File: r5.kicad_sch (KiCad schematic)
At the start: 73 parts, among them J1 Conn_01x04, U1 LMZ22005, U10 74368PW, U100 Pico, U2 74LS365, U20 DRV8871DDA, U3 GY-BNO08X, U30 DRV8871DDA, U4 PI22, U40 DRV8871DDA, U5 SDD1309, U50 DRV8871DDA, U6 3X3HEADER, U60 DRV8871DDA, U70 DRV8871DDA, U80 PCA9685PW, X1 Conn_01x02, X2 Conn_01x02, X20 Conn_01x06, X30 Conn_01x06, X40 Conn_01x06, X50 Conn_01x06, X60 Conn_01x06, X70 Conn_01x06, X81 4X3HEADER

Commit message: wip
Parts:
- added R15, R16, R17: 100k, Resistor_SMD:R_0805_2012Metric_Pad1.20x1.40mm_HandSolder, symbol Device:R
- added SW1, SW2, SW3, SW4: SW_SPDT, _r5:SW_Slide_1P2T_CK_OS102011MS2Q, symbol Switch:SW_SPDT
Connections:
- net +3.3V: now also R15.1, R16.1, R17.1
- net +BATT: now also SW1.3 (C); no longer R11.1
- net GND: now also SW3.1 (A), SW4.3 (C)
- net INBUTTON: now also R17.2
- net MENABLE: now also SW2.2 (B); no longer R10.2, U10.1 (OEa), U10.15 (OEb), U2.1 (E1), U2.15 (E2)
- net at U80.23 (~{OE}): now also R15.2, SW4.2 (B)
- net INWIFI: now reaches U4.11 (GPIO17)
- net INWIFI: now also R16.2, SW3.2 (B)
- new net: R10.2, SW2.3 (C), U10.1 (OEa), U10.15 (OEb), U2.1 (E1), U2.15 (E2)
- new net: R11.1, SW1.2 (B)
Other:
- moved on the sheet: C1, C2, R10, R11, R12, R13

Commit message: wip
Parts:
- D91: footprint LED_SMD:LED_WS2812B_PLCC4_5.0x5.0mm_P3.2mm -> LED_SMD:LED_WS2812B-2020_PLCC4_2.0x2.0mm; JLCPCB Rotation Offset (none) -> 0; LCSC Part # (none) -> C965555
- R10, R14, R15, R16, R17, R3: JLCPCB Rotation Offset (none) -> 0; LCSC Part # (none) -> C913998
- U20, U30, U40, U50, U60, U70: JLCPCB Rotation Offset (none) -> 0; LCSC Part # (none) -> C75864
- U80: JLCPCB Rotation Offset (none) -> 0; LCSC Part # (none) -> C2678753
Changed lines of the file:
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@@
       (effects (font (size 1.27 1.27)) hide)
     )
+    (property "JLCPCB Rotation Offset" "0" (at 355.6 364.49 0)
+      (effects (font (size 1.27 1.27)) hide)
+    )
+    (property "LCSC Part #" "C75864" (at 355.6 364.49 0)
+      (effects (font (size 1.27 1.27)) hide)
+    )
     (pin "6")
     (pin "2")
@@
       (effects (font (size 1.27 1.27)) hide)
     )
+    (property "JLCPCB Rotation Offset" "0" (at 355.6 400.05 0)
+      (effects (font (size 1.27 1.27)) hide)
+    )
+    (property "LCSC Part #" "C75864" (at 355.6 400.05 0)
+      (effects (font (size 1.27 1.27)) hide)
+    )
     (pin "1")
     (pin "7")
@@
       (effects (font (size 1.27 1.27)) hide)
     )
+    (property "JLCPCB Rotation Offset" "0" (at 411.48 327.66 0)
+      (effects (font (size 1.27 1.27)) hide)
+    )
+    (property "LCSC Part #" "C75864" (at 411.48 327.66 0)
+      (effects (font (size 1.27 1.27)) hide)
+    )
     (pin "1")
     (pin "2")
@@
       (effects (font (size 1.27 1.27)) hide)
     )
+    (property "JLCPCB Rotation Offset" "0" (at 411.48 363.22 0)
+      (effects (font (size 1.27 1.27)) hide)
+    )
+    (property "LCSC Part #" "C75864" (at 411.48 363.22 0)
+      (effects (font (size 1.27 1.27)) hide)
+    )
     (pin "7")
     (pin "5")
@@
       (effects (font (size 1.27 1.27)) hide)
     )
+    (property "JLCPCB Rotation Offset" "0" (at 411.48 400.05 0)
+      (effects (font (size 1.27 1.27)) hide)
+    )
+    (property "LCSC Part #" "C75864" (at 411.48 400.05 0)
+      (effects (font (size 1.27 1.27)) hide)
+    )
     (pin "7")
     (pin "6")
@@
       (effects (font (size 1.27 1.27)) hide)
     )
+    (property "LCSC Part #" "C2678753" (at 577.85 381 0)
+      (effects (font (size 1.27 1.27)) hide)
+    )
+    (property "JLCPCB Rotation Offset" "0" (at 577.85 381 0)
+      (effects (font (size 1.27 1.27)) hide)
+    )
     (pin "9")
     (pin "20")
@@
       (effects (font (size 1.27 1.27)) hide)
     )
+    (property "JLCPCB Rotation Offset" "0" (at 257.81 267.97 0)
+      (effects (font (size 1.27 1.27)) hide)
+    )
+    (property "LCSC Part #" "C913998" (at 257.81 267.97 0)
+      (effects (font (size 1.27 1.27)) hide)
+    )
     (pin "2")
     (pin "1")
@@
       (effects (font (size 1.27 1.27)) hide)
     )
+    (property "JLCPCB Rotation Offset" "0" (at 355.6 328.93 0)
+      (effects (font (size 1.27 1.27)) hide)
+    )
+    (property "LCSC Part #" "C75864" (at 355.6 328.93 0)
+      (effects (font (size 1.27 1.27)) hide)
+    )
     (pin "9")
     (pin "5")
@@
       (effects (font (size 1.27 1.27)) hide)
     )
+    (property "JLCPCB Rotation Offset" "0" (at 468.63 274.32 0)
+      (effects (font (size 1.27 1.27)) hide)
+    )
+    (property "LCSC Part #" "C913998" (at 468.63 274.32 0)
+      (effects (font (size 1.27 1.27)) hide)
+    )
     (pin "1")
     (pin "2")
@@
       (effects (font (size 1.27 1.27)) hide)
     )
-    (property "Footprint" "LED_SMD:LED_WS2812B_PLCC4_5.0x5.0mm_P3.2mm" (at 251.46 420.37 0)
+    (property "Footprint" "LED_SMD:LED_WS2812B-2020_PLCC4_2.0x2.0mm" (at 251.46 420.37 0)
       (effects (font (size 1.27 1.27)) hide)
     )
@@
       (effects (font (size 1.27 1.27)) hide)
     )
+    (property "JLCPCB Rotation Offset" "0" (at 251.46 420.37 0)
+      (effects (font (size 1.27 1.27)) hide)
+    )
+    (property "LCSC Part #" "C965555" (at 251.46 420.37 0)
+      (effects (font (size 1.27 1.27)) hide)
+    )
     (pin "1")
     (pin "4")
@@
       (effects (font (size 1.27 1.27)) hide)
     )
+    (property "JLCPCB Rotation Offset" "0" (at 546.1 345.44 0)
+      (effects (font (size 1.27 1.27)) hide)
+    )
+    (property "LCSC Part #" "C913998" (at 546.1 345.44 0)
+      (effects (font (size 1.27 1.27)) hide)
+    )
     (pin "1")
     (pin "2")
@@
       (effects (font (size 1.27 1.27)) hide)
     )
+    (property "JLCPCB Rotation Offset" "0" (at 509.27 203.2 0)
+      (effects (font (size 1.27 1.27)) hide)
+    )
+    (property "LCSC Part #" "C913998" (at 509.27 203.2 0)
+      (effects (font (size 1.27 1.27)) hide)
+    )
     (pin "1")
     (pin "2")
@@
       (effects (font (size 1.27 1.27)) hide)
     )
+    (property "JLCPCB Rotation Offset" "0" (at 543.56 260.35 0)
+      (effects (font (size 1.27 1.27)) hide)
+    )
+    (property "LCSC Part #" "C913998" (at 543.56 260.35 0)
+      (effects (font (size 1.27 1.27)) hide)
+    )
     (pin "1")
     (pin "2")
@@
       (effects (font (size 1.27 1.27)) hide)
     )
+    (property "JLCPCB Rotation Offset" "0" (at 306.07 407.67 0)
+      (effects (font (size 1.27 1.27)) hide)
+    )
+    (property "LCSC Part #" "C913998" (at 306.07 407.67 0)
+      (effects (font (size 1.27 1.27)) hide)
+    )

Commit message: wip
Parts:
- removed C1: 10u, Capacitor_SMD:C_1206_3216Metric_Pad1.33x1.80mm_HandSolder, symbol Device:C
- removed U10: 74368PW, Package_SO:TSSOP-16_4.4x5mm_P0.65mm, symbol 74xx:74LS368
- added J2: Conn_01x02, Connector_JST:JST_PH_B2B-PH-K_1x02_P2.00mm_Vertical, symbol Connector_Generic:Conn_01x02
- added R18: 300R, Resistor_SMD:R_0805_2012Metric, symbol Device:R
- added U7: 74HC540, Package_SO:TSSOP-20_4.4x6.5mm_P0.65mm, symbol 74xx:74LS540
- C10, C20, C30, C4, C40, C50, C60, C70, C90: footprint Capacitor_SMD:C_0805_2012Metric_Pad1.18x1.45mm_HandSolder -> Capacitor_SMD:C_0805_2012Metric; LCSC Part # (none) -> C49678
- C2: value 10u -> 22u; footprint Capacitor_SMD:C_1206_3216Metric_Pad1.33x1.80mm_HandSolder -> Capacitor_SMD:C_1206_3216Metric; LCSC Part # (none) -> C12891
- C21, C31, C41, C51, C61, C71: value CP -> 22u; footprint Capacitor_SMD:CP_Elec_5x5.7 -> Capacitor_SMD:C_1206_3216Metric; symbol Device:C_Polarized -> Device:C; LCSC Part # (none) -> C12891
- C3: LCSC Part # (none) -> C970695
- C80: value 10u -> 100n; footprint Capacitor_SMD:C_0805_2012Metric_Pad1.18x1.45mm_HandSolder -> Capacitor_SMD:C_0805_2012Metric; LCSC Part # (none) -> C49678
- C81: value CP -> 220u; footprint Capacitor_THT:CP_Radial_D6.3mm_P2.50mm -> Capacitor_SMD:CP_Elec_6.3x7.7; LCSC Part # (none) -> C970695
- D90: value DIODE-SOD523 -> 1N4148; footprint Diode_SMD:D_SOD-523 -> Diode_SMD:D_SOD-323; LCSC Part # (none) -> C2128
- D91: footprint LED_SMD:LED_WS2812B-2020_PLCC4_2.0x2.0mm -> LED_SMD:LED_WS2812B_PLCC4_5.0x5.0mm_P3.2mm; LCSC Part # C965555 -> (none)
- H1, H2, H3, H4, J1, SW1, SW2, SW3, SW4, U1, U100, U3, U4, U5, U6, X1, X2, X20, X30, X40, X50, X60, X70, X81: now left out of the parts list
- R1: footprint Resistor_SMD:R_0805_2012Metric_Pad1.20x1.40mm_HandSolder -> Resistor_SMD:R_0805_2012Metric; LCSC Part # (none) -> C17772
- R10, R14, R15, R16, R17, R3: footprint Resistor_SMD:R_0805_2012Metric_Pad1.20x1.40mm_HandSolder -> Resistor_SMD:R_0805_2012Metric; LCSC Part # C913998 -> C149504
- R11: footprint Resistor_SMD:R_0805_2012Metric_Pad1.20x1.40mm_HandSolder -> Resistor_SMD:R_0805_2012Metric; LCSC Part # (none) -> C40372
- R12: footprint Resistor_SMD:R_0805_2012Metric_Pad1.20x1.40mm_HandSolder -> Resistor_SMD:R_0805_2012Metric; LCSC Part # (none) -> C17448
- R13: footprint Resistor_SMD:R_0805_2012Metric_Pad1.20x1.40mm_HandSolder -> Resistor_SMD:R_0805_2012Metric; LCSC Part # (none) -> C17477
- R2: value 1k3 -> 1k; footprint Resistor_SMD:R_0805_2012Metric_Pad1.20x1.40mm_HandSolder -> Resistor_SMD:R_0805_2012Metric; LCSC Part # (none) -> C17513
- R20, R30, R4, R40, R50, R60, R70: value 33k -> 68k; footprint Resistor_SMD:R_0805_2012Metric_Pad1.20x1.40mm_HandSolder -> Resistor_SMD:R_0805_2012Metric; LCSC Part # (none) -> C17801
- R5, R6: value dnc -> ~; footprint Resistor_SMD:R_0805_2012Metric_Pad1.20x1.40mm_HandSolder -> Resistor_SMD:R_0805_2012Metric; now not fitted; now left out of the parts list
- R7, R8, R9: footprint Resistor_SMD:R_0805_2012Metric_Pad1.20x1.40mm_HandSolder -> Resistor_SMD:R_0805_2012Metric; LCSC Part # (none) -> C17673
- R90, R91: value 1k8 -> 4k7; footprint Resistor_SMD:R_0805_2012Metric_Pad1.20x1.40mm_HandSolder -> Resistor_SMD:R_0805_2012Metric; LCSC Part # (none) -> C17673
- U2: value 74LS365 -> 74HC365; LCSC Part # (none) -> C2675662
- U20, U30, U40, U50, U60, U70: JLCPCB Rotation Offset 0 -> -90
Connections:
- net +3.3V: now also U7.20 (VCC)
- net +5V: now also J2.1 (Pin_1)
- net GND: now also J2.2 (Pin_2), R18.2, U7.10 (GND), U7.8 (A6), U7.9 (A7); no longer C21.2, C31.2, C41.2, C51.2, C61.2, C71.2, R2.2, U20.7 (PGND), U30.7 (PGND), U40.7 (PGND), U50.7 (PGND), U60.7 (PGND), U70.7 (PGND)
- net IM1: now also U7.13 (Y5)
- net IM2: now also U7.18 (Y0)
- net IM3: now also U7.17 (Y1)
- net IM4: now also U7.16 (Y2)
- net IM5: now also U7.14 (Y4)
- net IM6: now also U7.15 (Y3)
- net M1: now also U7.7 (A5)
- net M2: now also U7.2 (A0)
- net M3: now also U7.3 (A1)
- net M4: now also U7.4 (A2)
- net M5: now also U7.6 (A4)
- net M6: now also U7.5 (A3)
- net at R10.2, SW2.3 (C), U2.1 (E1)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: now also U7.1 (G1), U7.19 (G2)
- new net: R18.1, R2.2
- new net GNDPWR: C21.2, C31.2, C41.2, C51.2, C61.2, C71.2, U20.7 (PGND), U30.7 (PGND), U40.7 (PGND), U50.7 (PGND), U60.7 (PGND), U70.7 (PGND)
- no-connect marks 22 -> 28
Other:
- note added: "0,94A current limmit set by 68k (Ilim=64000/R)"
- moved on the sheet: C10, C2, C20, C3, C30, C4, C40, C50, C60, C70, C80, C81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

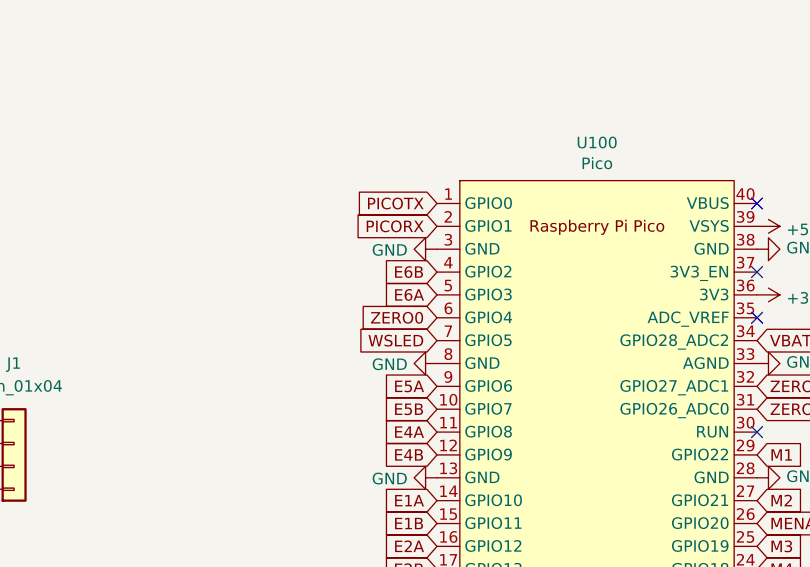
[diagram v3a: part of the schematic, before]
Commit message: component placement
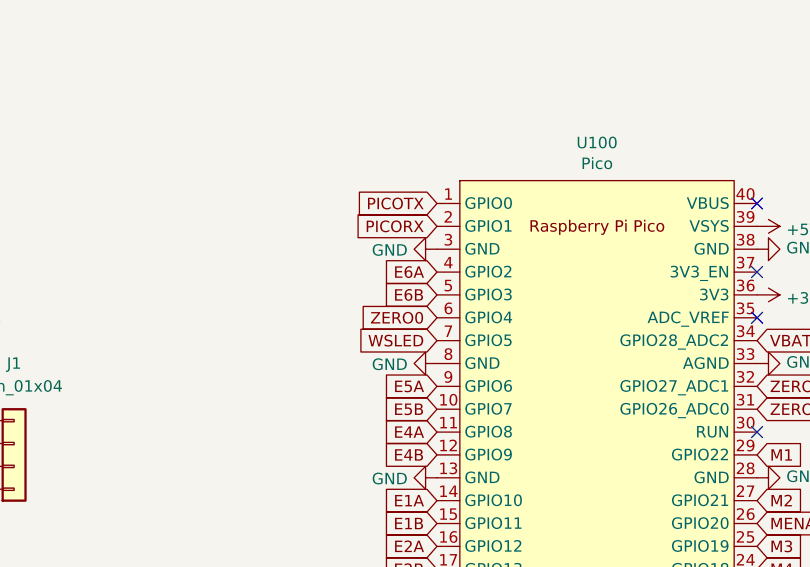
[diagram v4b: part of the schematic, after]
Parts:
- D91: now left out of the parts list
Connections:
- net E6A: now also U100.4 (GPIO2); no longer U100.5 (GPIO3)
- net E6B: now also U100.5 (GPIO3); no longer U100.4 (GPIO2)
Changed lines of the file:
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@@
     )
   )
-  (global_label "E6A" (shape input) (at 175.26 182.88 180)
+  (global_label "E6A" (shape input) (at 175.26 180.34 180)
     (effects (font (size 1.27 1.27)) (justify right))
-    (property "Intersheetrefs" "${INTERSHEET_REFS}" (at 175.26 182.88 0)
+    (property "Intersheetrefs" "${INTERSHEET_REFS}" (at 175.26 180.34 0)
       (effects (font (size 1.27 1.27)) hide)
     )
@@
     )
   )
-  (global_label "E6B" (shape input) (at 175.26 180.34 180)
+  (global_label "E6B" (shape input) (at 175.26 182.88 180)
     (effects (font (size 1.27 1.27)) (justify right))
-    (property "Intersheetrefs" "${INTERSHEET_REFS}" (at 175.26 180.34 0)
+    (property "Intersheetrefs" "${INTERSHEET_REFS}" (at 175.26 182.88 0)
       (effects (font (size 1.27 1.27)) hide)
     )
@@
   )
   (symbol (lib_id "LED:WS2812B") (at 69.85 204.47 0) (unit 1)
-    (in_bom yes) (on_board yes) (dnp no)
+    (in_bom no) (on_board yes) (dnp no)
     (property "Reference" "D91" (at 69.85 204.47 0)
       (effects (font (size 1.27 1.27)) hide)

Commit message: positions
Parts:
- removed R17: 100k, Resistor_SMD:R_0805_2012Metric, symbol Device:R
- D41: renamed from D91; JLCPCB Rotation Offset 0 -> (none)
- R16: renamed from R3; JLCPCB Rotation Offset 0 -> (none)
- R40: renamed from R14; JLCPCB Rotation Offset 0 -> (none)
- R60: renamed from R15; JLCPCB Rotation Offset 0 -> (none)
- R70: renamed from R10; JLCPCB Rotation Offset 0 -> (none)
- R80: renamed from R16; JLCPCB Rotation Offset 0 -> (none)
- U60: renamed from U80; JLCPCB Rotation Offset 0 -> (none)
- U70: renamed from U2; JLCPCB Rotation Offset (none) -> -90
- U71: renamed from U7; JLCPCB Rotation Offset (none) -> -90
- renumbered C2 to C10, C3 to C11, C30 to C21, C40 to C22, C21 to C23, C31 to C24, C41 to C25, C50 to C26, C60 to C27, C70 to C28, C51 to C29, C61 to C30, C71 to C31, C90 to C40, C80 to C60, C4 to C70, C10 to C71, C81 to C90, D90 to D40, H1 to H201, H2 to H202, H3 to H203, H4 to H204, R11 to R10, R12 to R11, R13 to R12, R1 to R13, R2 to R14, R18 to R15, R4 to R17, R30 to R21, R40 to R22, R50 to R23, R60 to R24, R70 to R25, R5 to R61, R6 to R62, R7 to R90, R8 to R91, R9 to R92, R90 to R93, R91 to R94, SW1 to SW10, SW4 to SW60, SW2 to SW70, SW3 to SW80, U1 to U10, U30 to U21, U40 to U22, U50 to U23, U60 to U24, U70 to U25, U4 to U50, U100 to U80, X1 to X10, X2 to X11, J2 to X12, X30 to X21, X40 to X22, X50 to X23, X60 to X24, X70 to X25, J1 to X40, U6 to X90, X81 to X91, U5 to X92, U3 to X93
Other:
- moved on the sheet: C60, R61, R62, R80, R93, R94, SW80

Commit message: start routing
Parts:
- removed U70: 74HC365, Package_SO:TSSOP-16_4.4x5mm_P0.65mm, symbol 74xx:74LS365
- added U51: 74HC541, Package_SO:TSSOP-20_4.4x6.5mm_P0.65mm, symbol 74xx:74LS541
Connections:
- net +3.3V: now also U51.20 (VCC)
- net E1A: now also U80.6 (GPIO4); no longer U80.14 (GPIO10)
- net E1B: now also U80.7 (GPIO5); no longer U80.15 (GPIO11)
- net E2A: now also U80.9 (GPIO6); no longer U80.16 (GPIO12)
- net E2B: now also U80.10 (GPIO7); no longer U80.17 (GPIO13)
- net E3A: now also U80.11 (GPIO8); no longer U80.19 (GPIO14)
- net E3B: now also U80.12 (GPIO9); no longer U80.20 (GPIO15)
- net E4A: now also U80.14 (GPIO10); no longer U80.11 (GPIO8)
- net E4B: now also U80.15 (GPIO11); no longer U80.12 (GPIO9)
- net E5A: now also U80.16 (GPIO12); no longer U80.9 (GPIO6)
- net E5B: now also U80.17 (GPIO13); no longer U80.10 (GPIO7)
- net E6A: now also U80.19 (GPIO14); no longer U80.4 (GPIO2)
- net E6B: now also U80.20 (GPIO15); no longer U80.5 (GPIO3)
- net EM1: now also U51.18 (Y0)
- net EM2: now also U51.17 (Y1)
- net EM3: now also U51.16 (Y2)
- net EM4: now also U51.15 (Y3)
- net EM5: now also U51.14 (Y4)
- net EM6: now also U51.13 (Y5)
- net GND: now also U51.10 (GND), U51.8 (A6), U51.9 (A7)
- net IM2: now also U71.14 (Y4); no longer U71.18 (Y0)
- net IM3: now also U71.15 (Y3); no longer U71.17 (Y1)
- net IM5: now also U71.17 (Y1); no longer U71.14 (Y4)
- net IM6: now also U71.18 (Y0); no longer U71.15 (Y3)
- net M1: now also U80.27 (GPIO21), U51.2 (A0); no longer U80.29 (GPIO22)
- net M2: now also U71.6 (A4), U80.26 (GPIO20), U51.3 (A1); no longer U71.2 (A0), U80.27 (GPIO21)
- net M3: now also U71.5 (A3), U51.4 (A2); no longer U71.3 (A1)
- net M4: now also U80.21 (GPIO16), U51.5 (A3); no longer U80.24 (GPIO18)
- net M5: now also U71.3 (A1), U51.6 (A4); no longer U71.6 (A4)
- net M6: now also U71.2 (A0), U80.24 (GPIO18), U51.7 (A5); no longer U71.5 (A3), U80.21 (GPIO16)
- net MENABLE: now also U80.29 (GPIO22); no longer U80.26 (GPIO20)
- net WSLED: now also U80.5 (GPIO3); no longer U80.7 (GPIO5)
- net ZERO0: now also U80.4 (GPIO2); no longer U80.6 (GPIO4)
- net at R70.2, SW70.3 (C), U71.1 (G1)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: now also U51.1 (G1), U51.19 (G2)
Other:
- moved on the sheet: C70, R70
